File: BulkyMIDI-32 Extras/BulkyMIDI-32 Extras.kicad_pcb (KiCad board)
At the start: 2 copper layers, 100 x 100 mm, 66 parts, among them J1 DC IN, J10 MIDI2, J11 MIDI3, J12 SERIAL, J13 ICSP, J14 BIN/ASCII, J15 BAUD_RATE, J16 Stacked RS232 Module, J2 MIDI OUT, J3 MIDI IN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

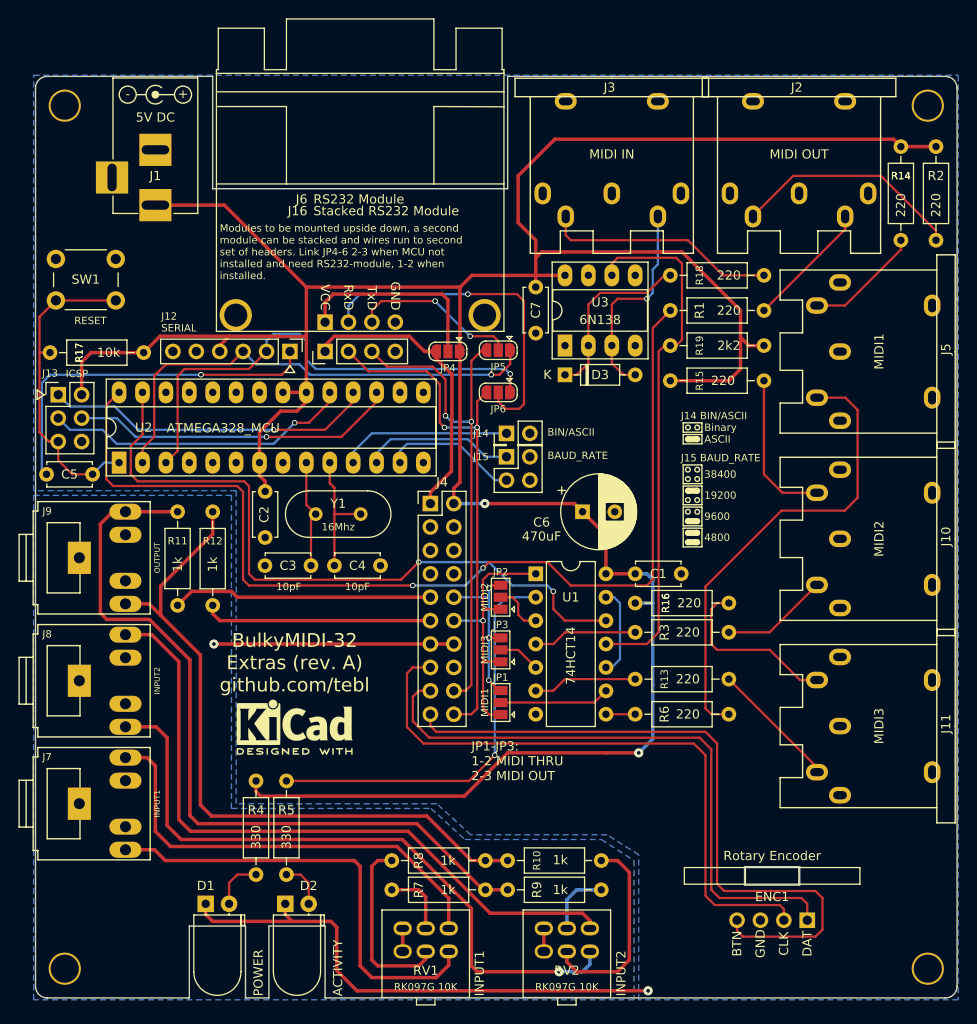
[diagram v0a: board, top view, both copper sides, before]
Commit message: Add third status LED
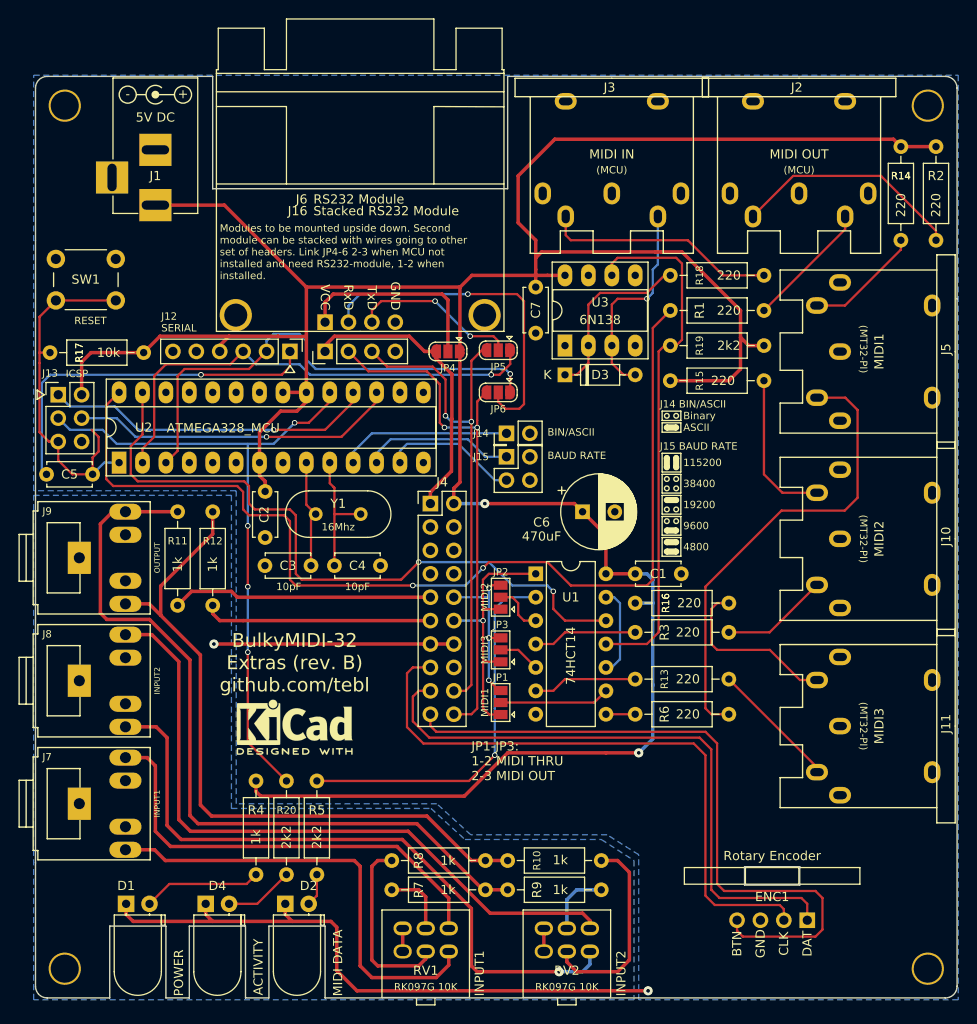
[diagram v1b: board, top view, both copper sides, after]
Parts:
- added D4: ACTIVITY, LED_THT:LED_D5.0mm_Horizontal_O1.27mm_Z3.0mm, F.Cu at (88.6, 144.4)
- added R20: 2k2, Resistor_THT:R_Axial_DIN0207_L6.3mm_D2.5mm_P10.16mm_Horizontal, F.Cu at (97.4, 141.2)
- D2: value ACTIVITY -> MIDI DATA
- J15: value BAUD_RATE -> BAUD RATE
- R4: value 330 -> 1k
- R5: value 330 -> 2k2
- moved D1 8.64 mm to (80.0, 144.4)
- moved R5 3.30 mm to (100.7, 141.2)
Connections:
- net Net-(J13-Pad3) renamed MCU_LED
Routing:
- net MCU_LED: track 33.5 -> 71.8 mm, vias 1 -> 4
- net GND: track 58.2 -> 69.0 mm
- net Net-(D4-Pad2): track 0.00 -> 7.54 mm
- net Net-(D1-Pad2): track 5.58 -> 12.9 mm
- net /~RESET: track 34.9 -> 40.3 mm
- net Net-(R5-Pad2): track 44.6 -> 41.3 mm
- net Net-(D2-Pad2): track 5.07 -> 3.54 mm
- net MIDI_OUT: track 112.0 -> 111.3 mm
- net MIDI_IN: track 75.8 -> 75.1 mm
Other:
- outline, holes or cut-outs redrawn
- board text added: "(MCU)"
- board text added: "(MT32-PI)"
- board text added: "115200"
- board text added: "BulkyMIDI-32 Extras (rev. B) github.com/tebl"
- board text added: "J15 BAUD RATE"
- board text added: "MIDI IN (MCU)"
- board text added: "MIDI OUT (MCU)"
- board text added: "MIDI1 (MT-32)"
- board text added: "MIDI2 (MT-32)"
- board text added: "MIDI3 (MT-32)"
- board text added: "Modules to be mounted upside down. Second module can be stacked with wires going to other set of headers. Link JP4-6 2-3 when MCU not installed and need RS232-module, 1-2 when installed."
- board text removed: "BulkyMIDI-32 Extras (rev. A) github.com/tebl"
- board text removed: "J15 BAUD_RATE"
- board text removed: "MIDI IN"
- board text removed: "MIDI OUT"
- board text removed: "MIDI1"
- board text removed: "MIDI2"
- board text removed: "MIDI3"
- board text removed: "Modules to be mounted upside down, a second module can be stacked and wires run to second set of headers. Link JP4-6 2-3 when MCU not installed and need RS232-module, 1-2 when installed."

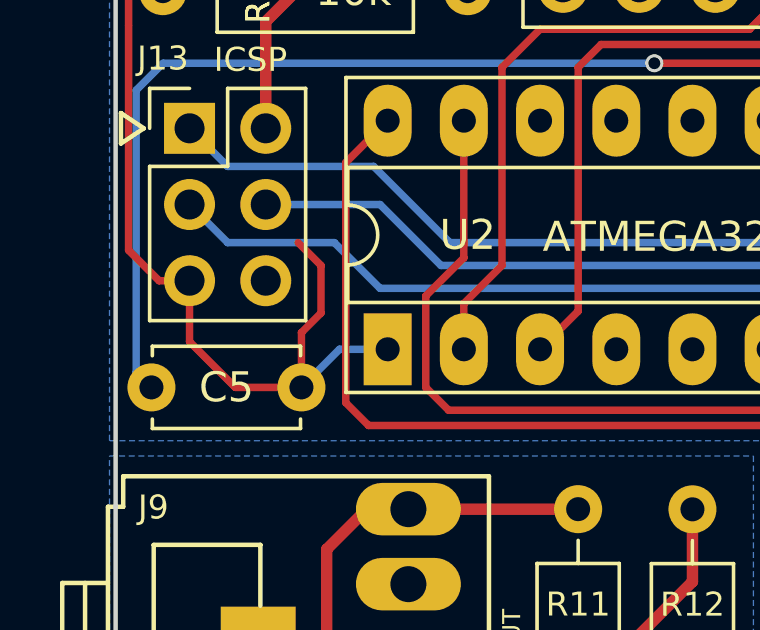
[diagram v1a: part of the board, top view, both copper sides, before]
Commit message: Removed loose track
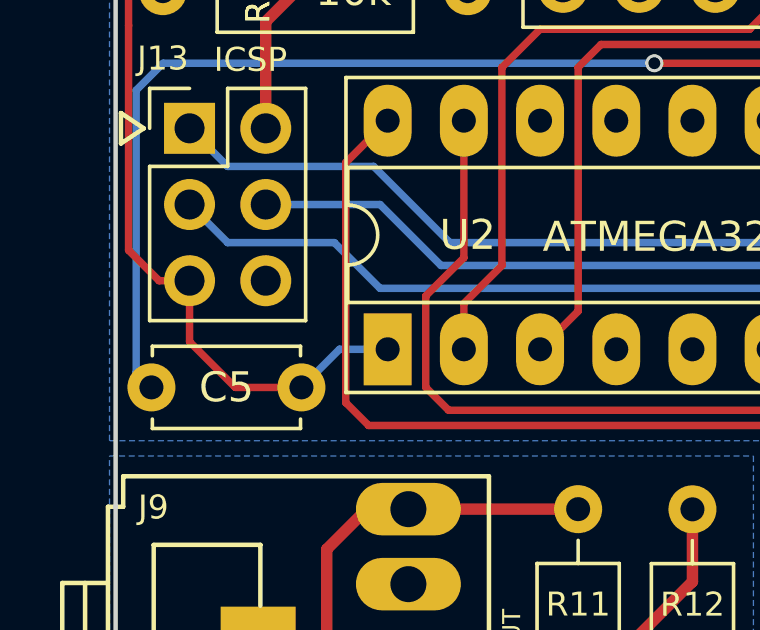
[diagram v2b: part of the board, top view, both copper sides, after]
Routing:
- net /~RESET: track 40.3 -> 34.9 mm
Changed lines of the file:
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@@
     (thickness 1.6)
     (drawings 141)
-    (tracks 595)
+    (tracks 591)
     (zones 0)
     (modules 68)
@@
   (segment (start 70.612 84.582) (end 70.612 80.7) (width 0.25) (layer F.Cu) (net 40))
   (segment (start 70.612 85.725) (end 70.612 84.582) (width 0.25) (layer F.Cu) (net 40))
-  (segment (start 76.374 97.79) (end 76.374 95.965) (width 0.25) (layer F.Cu) (net 40))
-  (segment (start 76.374 95.965) (end 77.0255 95.3135) (width 0.25) (layer F.Cu) (net 40))
-  (segment (start 77.0255 95.3135) (end 77.0255 93.726) (width 0.25) (layer F.Cu) (net 40))
-  (segment (start 77.0255 93.726) (end 76.2635 92.964) (width 0.25) (layer F.Cu) (net 40))
   (segment (start 71.628 94.234) (end 70.612 93.218) (width 0.25) (layer F.Cu) (net 40))
   (segment (start 72.644 94.234) (end 71.628 94.234) (width 0.25) (layer F.Cu) (net 40) (status 10))
-  (segment (start 74.168 97.79) (end 72.644 96.266) (width 0.25) (layer F.Cu) (net 40) (status 1000000))
-  (segment (start 72.644 96.266) (end 72.644 94.234) (width 0.25) (layer F.Cu) (net 40) (status 1000020))
-  (segment (start 76.374 97.79) (end 74.168 97.79) (width 0.25) (layer F.Cu) (net 40) (status 1000010))
+  (segment (start 74.168 97.79) (end 72.644 96.266) (width 0.25) (layer F.Cu) (net 40))
+  (segment (start 72.644 96.266) (end 72.644 94.234) (width 0.25) (layer F.Cu) (net 40) (status 20))
+  (segment (start 76.374 97.79) (end 74.168 97.79) (width 0.25) (layer F.Cu) (net 40) (status 10))
   (segment (start 70.612 93.218) (end 70.612 85.725) (width 0.25) (layer F.Cu) (net 40))
   (via (at 88.138 86.985) (size 0.6) (drill 0.4) (layers F.Cu B.Cu) (net 41))

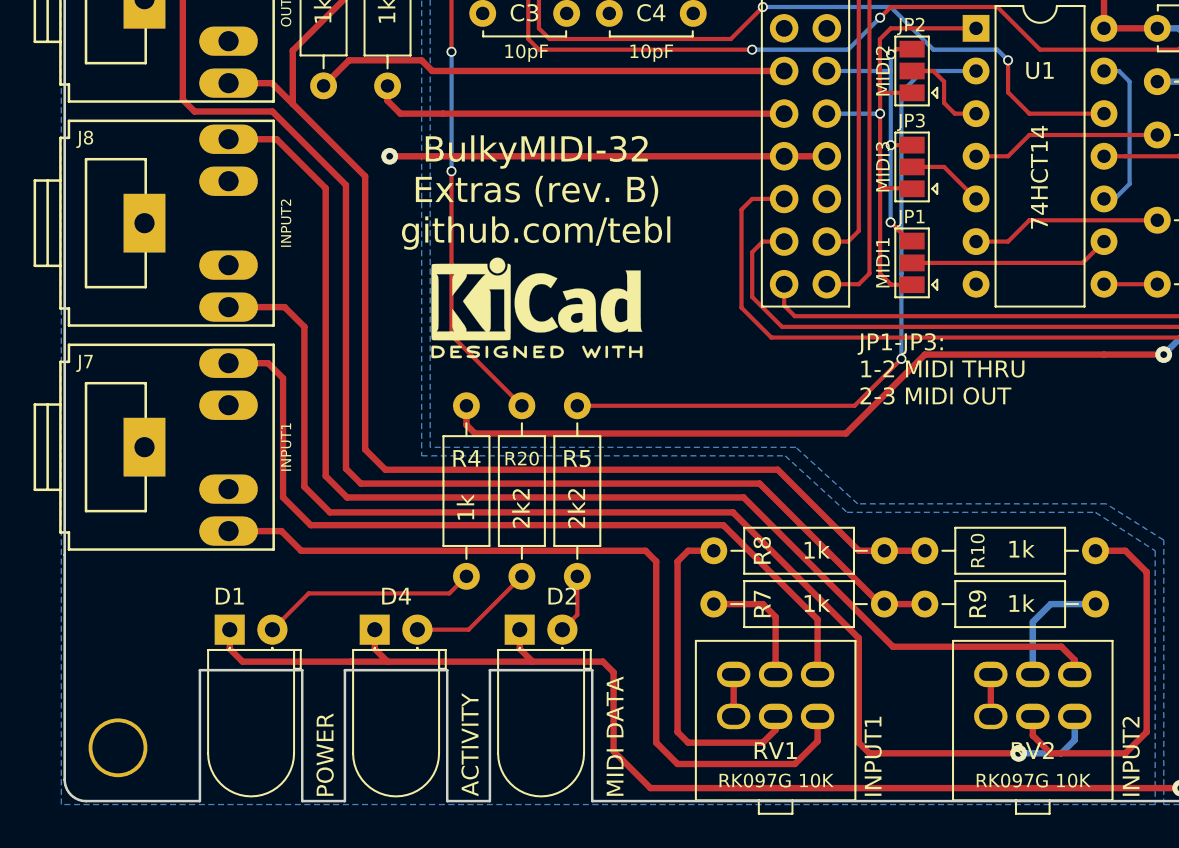
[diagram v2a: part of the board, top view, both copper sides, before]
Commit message: Swapped INPUT1/INPUT2 inputs
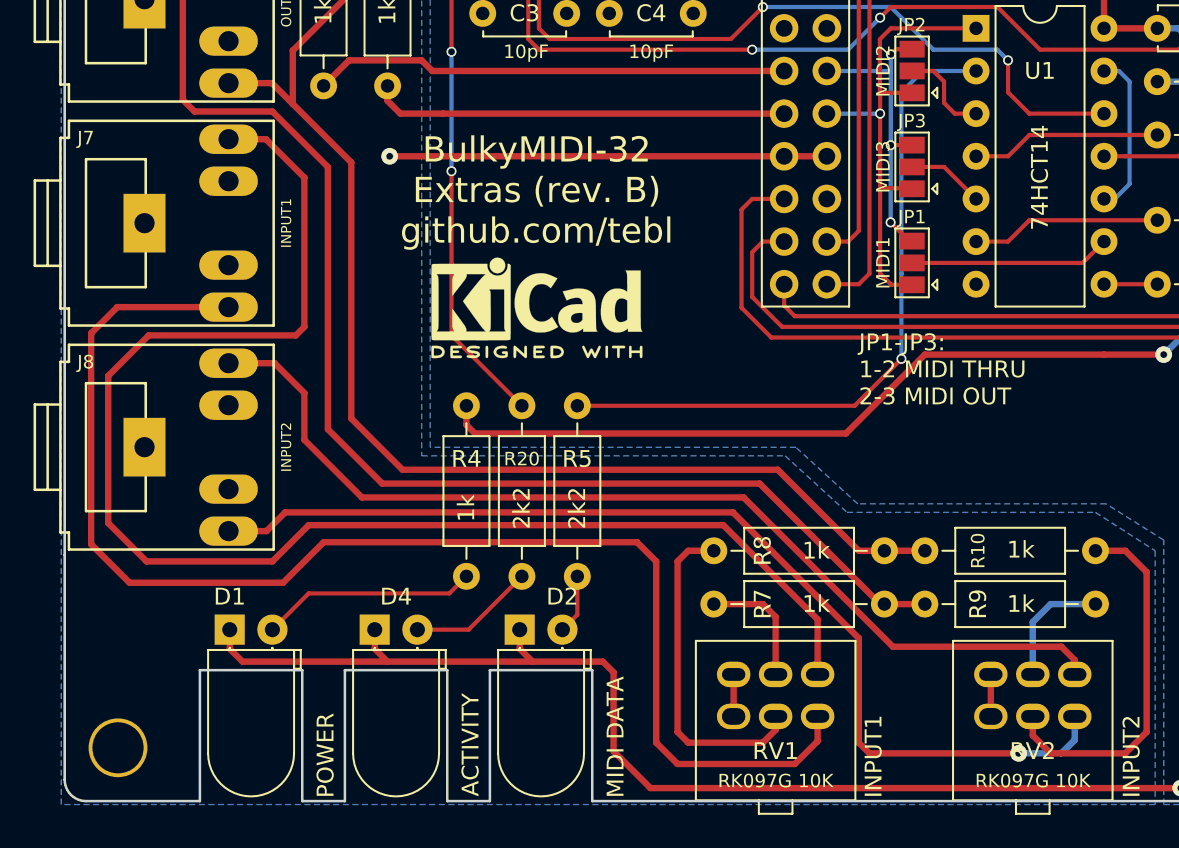
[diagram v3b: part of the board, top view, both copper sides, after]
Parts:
- moved J7 13.3 mm to (76.5, 120.2)
- moved J8 13.3 mm to (76.5, 133.5)
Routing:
- net /I1_R: track 48.8 -> 85.7 mm
- net /I1_L: track 49.2 -> 80.4 mm
- net /I2_R: track 74.1 -> 60.2 mm
- net /I2_L: track 72.4 -> 62.2 mm
- net /RIGHT: track 85.1 -> 84.4 mm
- net /LEFT: track 76.1 -> 75.5 mm

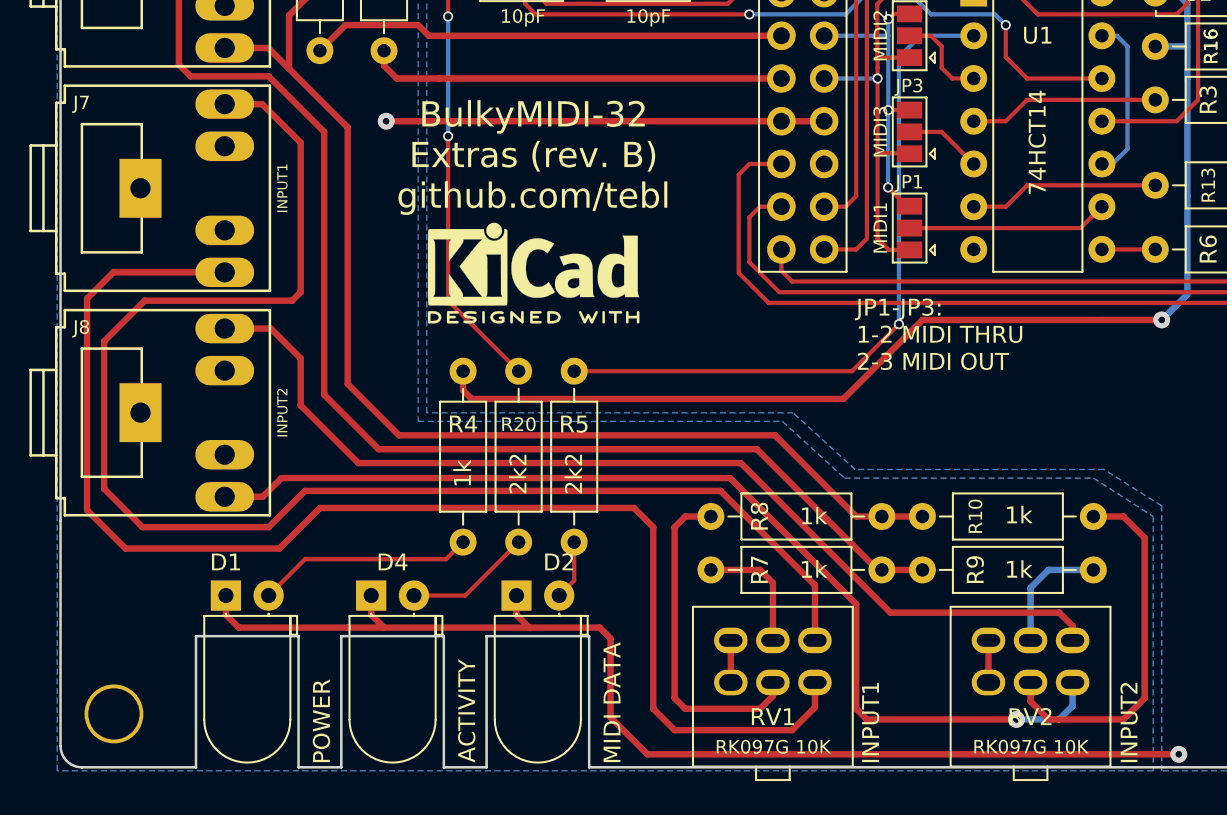
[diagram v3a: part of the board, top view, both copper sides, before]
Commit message: Slightly recessed potentiometers
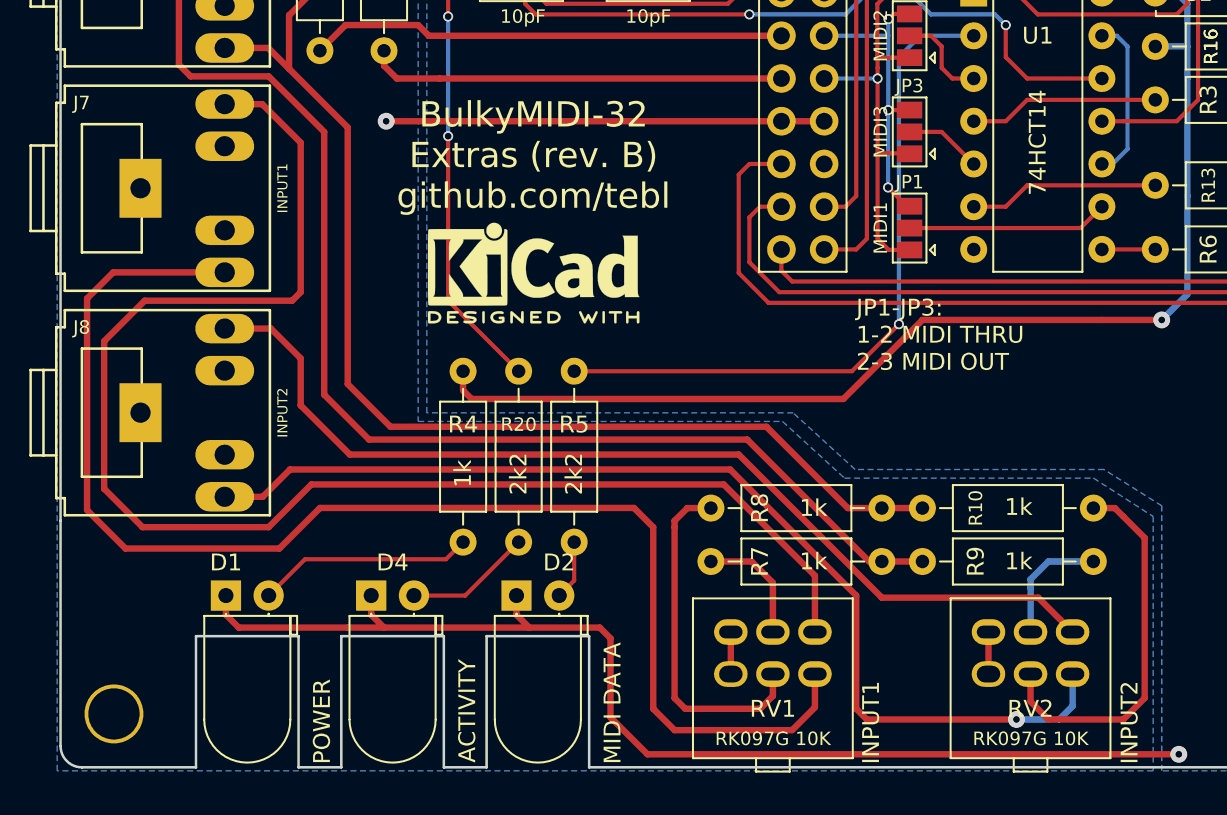
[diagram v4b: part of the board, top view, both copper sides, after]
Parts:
- moved R10 0.50 mm to (131.6, 139.2)
- moved R7 0.50 mm to (119.0, 142.4)
- moved R8 0.50 mm to (108.8, 139.2)
- moved R9 0.50 mm to (121.4, 142.4)
- moved RV1 0.50 mm to (112.5, 146.6)
- moved RV2 0.50 mm to (127.8, 146.6)
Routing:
- net /I2_L: track 62.2 -> 63.4 mm
- net Net-(R8-Pad1): track 19.8 -> 20.7 mm
- net /I2_R: track 60.2 -> 59.5 mm
- net Net-(R10-Pad1): track 22.1 -> 22.7 mm
- net /I1_L: track 80.4 -> 80.9 mm
